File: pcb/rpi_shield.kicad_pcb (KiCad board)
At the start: 2 copper layers, 65 x 56 mm, 60 parts, among them P101 CONN_01X08, P102 CONN_02X20, P301 USB_OTG, Q201 Q_NMOS_GDSD, Q202 Q_NMOS_GDSD, Q203 Q_NMOS_GDSD, Q204 Q_NMOS_GDSD, Q301 FT230XS-R, U201 LM2902N, U202 MAX5813

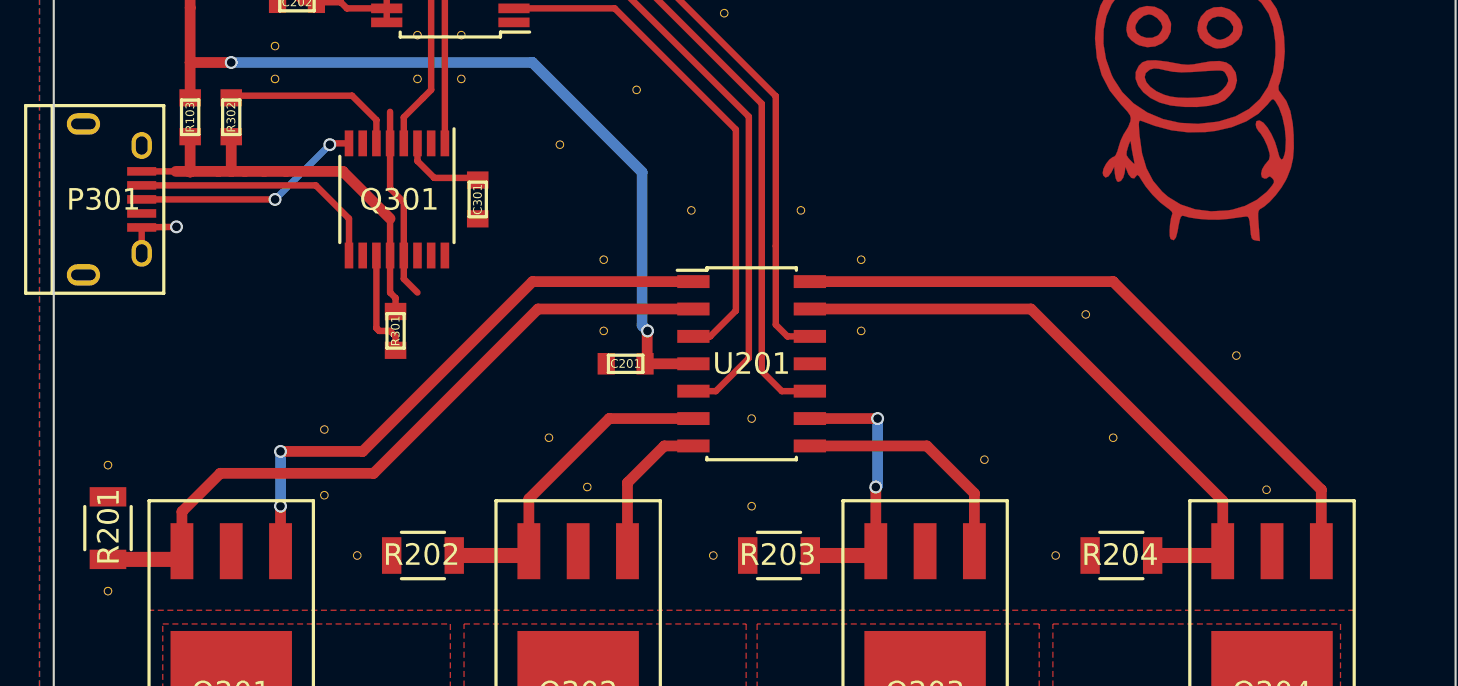
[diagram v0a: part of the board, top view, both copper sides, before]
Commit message: added gain to current feedback
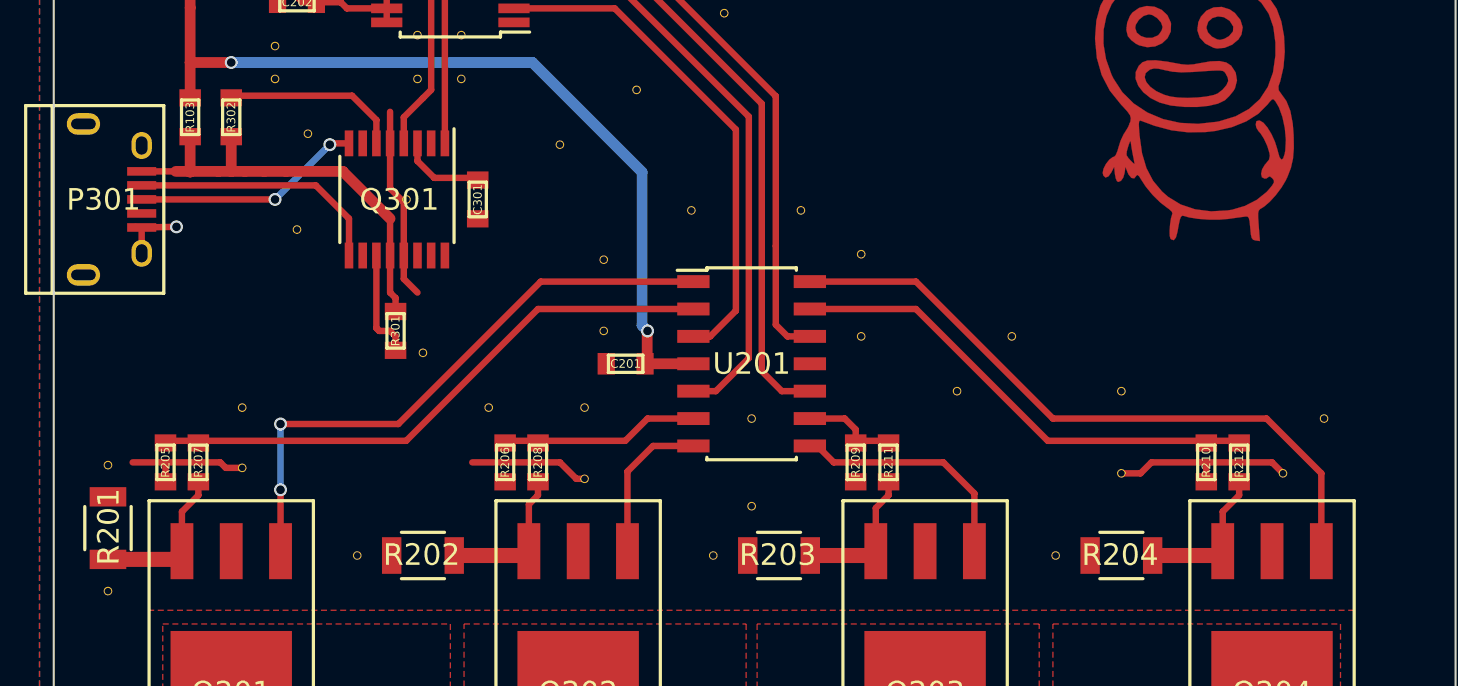
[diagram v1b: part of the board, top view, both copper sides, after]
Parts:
- removed the VIA at (144.7, 106.3)
- removed the VIA at (164.9, 107.3)
- removed the VIA at (170.9, 106.3)
- removed the VIA at (176.6, 102.5)
- removed the VIA at (146.5, 108.6)
- removed the VIA at (178.0, 108.7)
- removed the VIA at (134.3, 105.9)
- removed the VIA at (134.3, 109.0)
- added R205: 1k, netl:SMD_0603, F.Cu at (127.0, 107.4)
- added R206: 1k, netl:SMD_0603, F.Cu at (142.7, 107.4)
- added R207: 10k, netl:SMD_0603, F.Cu at (128.5, 107.4)
- added R208: 10k, netl:SMD_0603, F.Cu at (144.2, 107.4)
- added R209: 1k, netl:SMD_0603, F.Cu at (159.0, 107.4)
- added R210: 1k, netl:SMD_0603, F.Cu at (175.2, 107.4)
- added R211: 10k, netl:SMD_0603, F.Cu at (160.5, 107.4)
- added R212: 10k, netl:SMD_0603, F.Cu at (176.7, 107.4)
- added VIA: via, netl:via, F.Cu at (133.0, 96.6)
- added VIA: via, netl:via, F.Cu at (146.4, 108.2)
- added VIA: via, netl:via, F.Cu at (141.9, 104.9)
- added VIA: via, netl:via, F.Cu at (138.9, 102.4)
- added VIA: via, netl:via, F.Cu at (138.1, 95.2)
- added VIA: via, netl:via, F.Cu at (133.6, 92.2)
- added VIA: via, netl:via, F.Cu at (146.4, 104.9)
- added VIA: via, netl:via, F.Cu at (180.7, 105.4)
- added VIA: via, netl:via, F.Cu at (178.8, 107.9)
- added VIA: via, netl:via, F.Cu at (171.3, 104.1)
- added VIA: via, netl:via, F.Cu at (171.3, 107.9)
- added VIA: via, netl:via, F.Cu at (163.7, 104.1)
- added VIA: via, netl:via, F.Cu at (130.5, 104.9)
- added VIA: via, netl:via, F.Cu at (130.5, 107.7)
- moved VIA 3.58 mm to (166.2, 101.6)
- moved VIA 0.25 mm to (159.2, 97.8)
- moved VIA 0.25 mm to (159.2, 101.6)
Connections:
- U201 pad 13: Net-(Q204-Pad3) -> Net-(R210-Pad1)
- U201 pad 2: Net-(Q201-Pad3) -> Net-(R205-Pad1)
- U201 pad 6: Net-(Q202-Pad3) -> Net-(R206-Pad1)
- U201 pad 9: Net-(Q203-Pad3) -> Net-(R209-Pad1)
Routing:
- net Net-(R205-Pad1): track 0.00 -> 27.0 mm
- net Net-(Q201-Pad3): track 33.3 -> 7.26 mm
- net Net-(R210-Pad1): track 0.00 -> 22.4 mm
- net Net-(Q204-Pad3): track 29.2 -> 7.44 mm
- net GND: track 24.3 -> 44.9 mm
- net Net-(R206-Pad1): track 0.00 -> 9.16 mm
- net Net-(Q202-Pad3): track 15.3 -> 6.99 mm
- net Net-(Q203-Pad3): track 13.5 -> 7.57 mm, vias 2 -> 0
- net Net-(R209-Pad1): track 0.00 -> 4.38 mm
- net Net-(Q201-Pad1): track 27.4 -> 28.1 mm

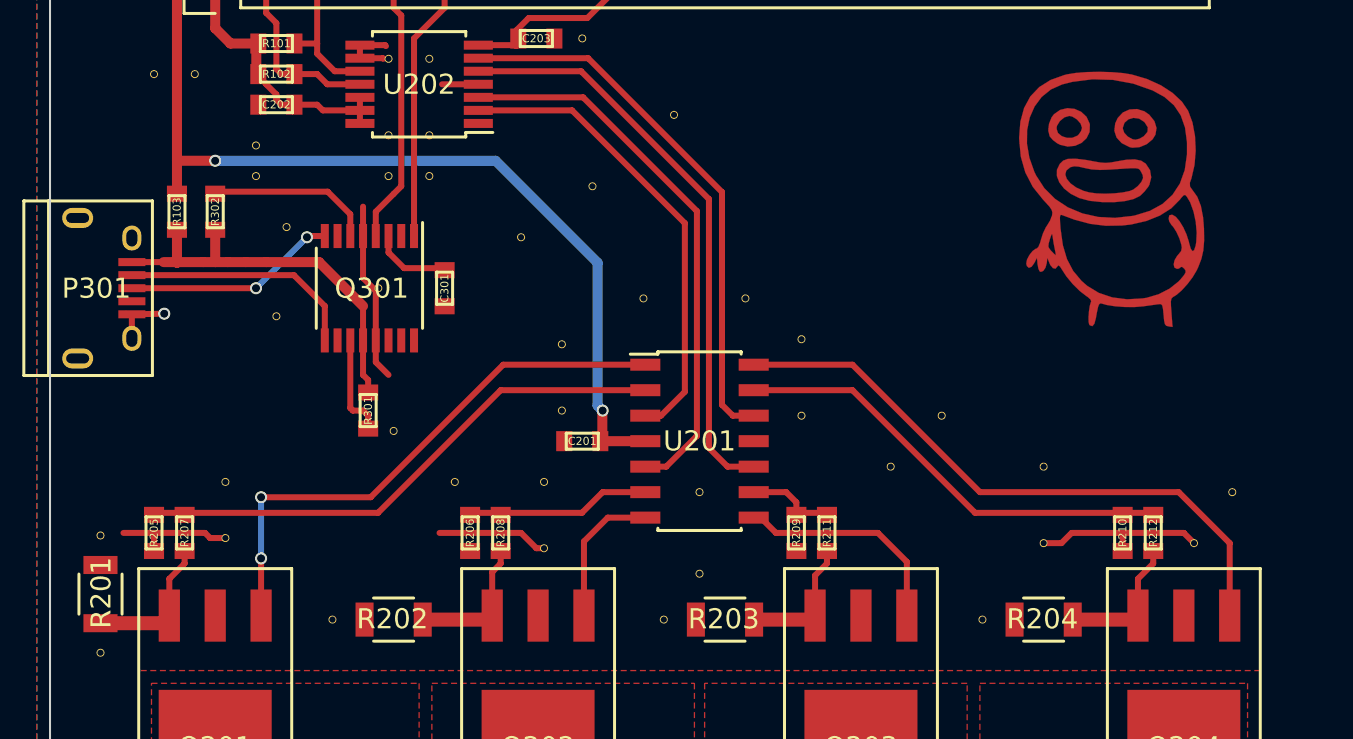
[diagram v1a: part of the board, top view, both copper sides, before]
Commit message: removed gain from feedback, added adjust to DAC reference voltage
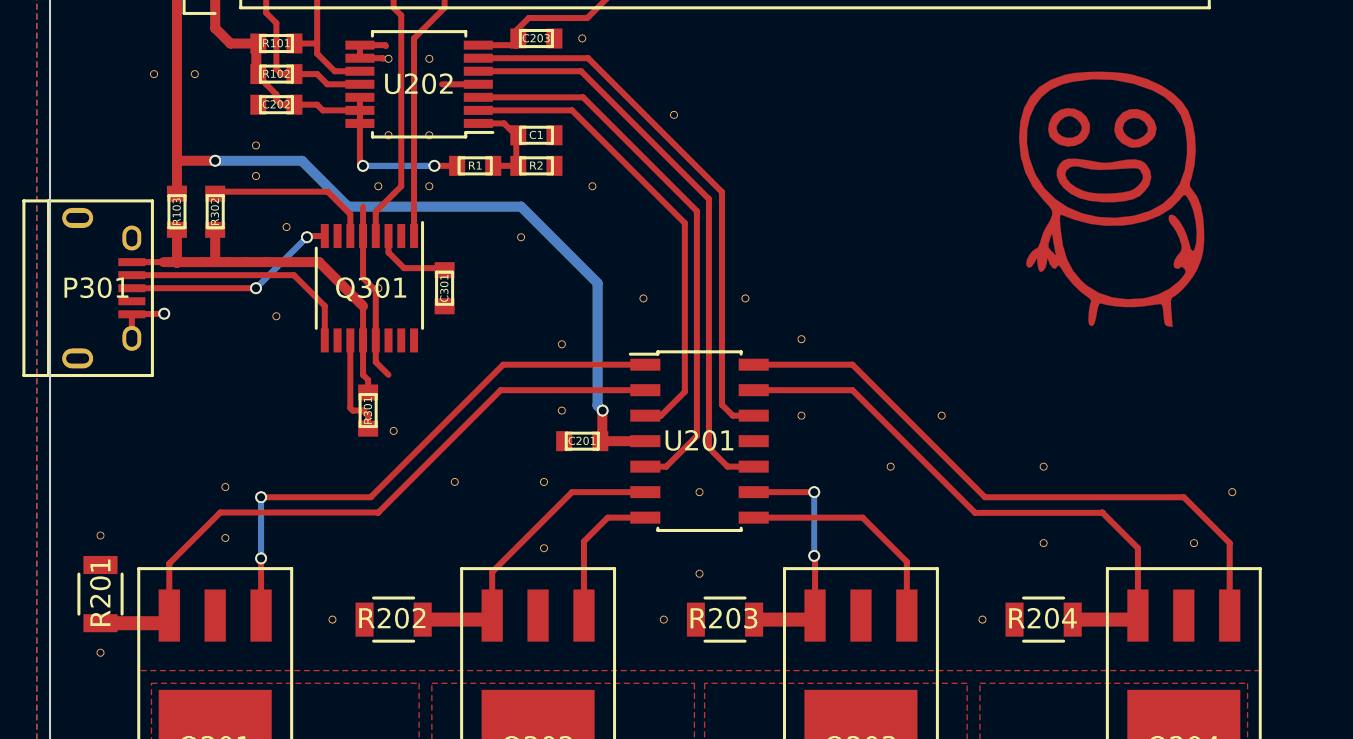
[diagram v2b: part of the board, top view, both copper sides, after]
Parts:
- removed R205, R206, R209, R210: 1k, netl:SMD_0603
- removed R207, R208, R211, R212: 10k, netl:SMD_0603
- added C1: 100n, netl:SMD_0603, F.Cu at (146.0, 87.6)
- added R1: 20k, netl:SMD_0603, F.Cu at (143.0, 89.1)
- added R2: 10k, netl:SMD_0603, F.Cu at (146.0, 89.1)
- moved VIA 0.72 mm to (138.1, 90.2)
- moved VIA 0.51 mm to (140.7, 90.2)
- moved VIA 0.25 mm to (130.5, 105.1)
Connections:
- U201 pad 13: Net-(R210-Pad1) -> Net-(Q204-Pad3)
- U201 pad 2: Net-(R205-Pad1) -> Net-(Q201-Pad3)
- U201 pad 6: Net-(R206-Pad1) -> Net-(Q202-Pad3)
- U201 pad 9: Net-(R209-Pad1) -> Net-(Q203-Pad3)
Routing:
- net Net-(R205-Pad1): track 27.0 -> 0.00 mm
- net Net-(Q201-Pad3): track 7.26 -> 33.7 mm
- net Net-(R210-Pad1): track 22.4 -> 0.00 mm
- net Net-(Q204-Pad3): track 7.44 -> 29.8 mm
- net GND: track 44.9 -> 24.3 mm
- net Net-(R206-Pad1): track 9.16 -> 0.00 mm
- net Net-(Q202-Pad3): track 6.99 -> 15.1 mm
- net 3v3: track 22.6 -> 29.4 mm, vias 0 -> 2
- net Net-(Q203-Pad3): track 7.57 -> 13.4 mm, vias 0 -> 2
- net Net-(C1-Pad2): track 0.00 -> 4.71 mm
- net Net-(R209-Pad1): track 4.38 -> 0.00 mm
- net 5V: track 51.2 -> 50.7 mm

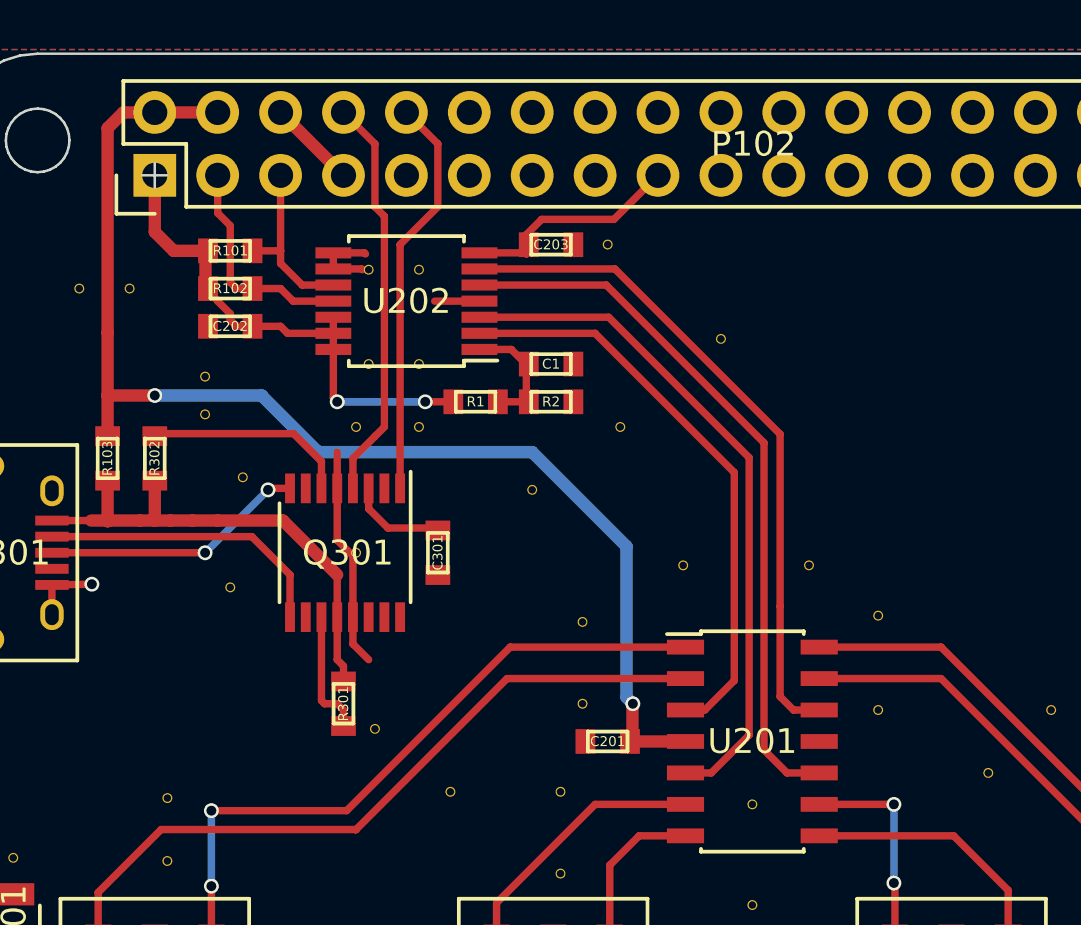
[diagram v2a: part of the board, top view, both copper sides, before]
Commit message: added pulldown transistors, moved reference adjust to DAC output
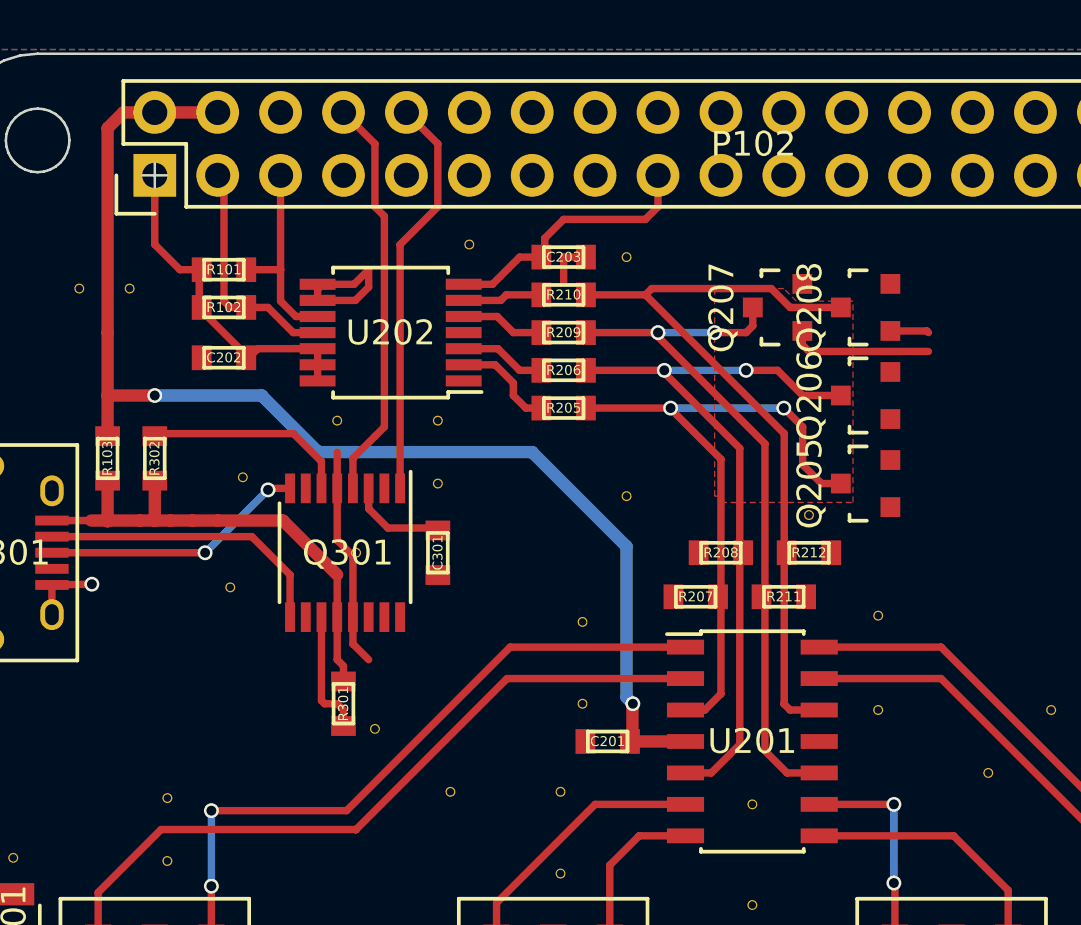
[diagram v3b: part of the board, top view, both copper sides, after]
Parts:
- removed C1: 100n, netl:SMD_0603
- removed R1: 20k, netl:SMD_0603
- removed R2: 10k, netl:SMD_0603
- removed the VIA at (145.2, 92.7)
- removed the VIA at (132.0, 88.1)
- removed the VIA at (132.0, 89.7)
- removed the VIA at (140.7, 87.6)
- removed the VIA at (138.6, 87.6)
- removed the VIA at (148.8, 90.2)
- removed the VIA at (152.9, 86.6)
- removed the VIA at (148.3, 82.8)
- removed the VIA at (138.6, 83.8)
- added Q205: NPN, TO_SOT_Packages_SMD:SOT-23, F.Cu at (158.7, 92.4)
- added Q206: NPN, TO_SOT_Packages_SMD:SOT-23, F.Cu at (158.7, 88.9)
- added Q207: NPN, TO_SOT_Packages_SMD:SOT-23, F.Cu at (155.1, 85.3)
- added Q208: NPN, TO_SOT_Packages_SMD:SOT-23, F.Cu at (158.7, 85.3)
- added R205: 10k, netl:SMD_0603, F.Cu at (146.5, 89.4)
- added R206: 10k, netl:SMD_0603, F.Cu at (146.5, 87.9)
- added R207: 10k, netl:SMD_0603, F.Cu at (151.8, 97.0)
- added R208: 10k, netl:SMD_0603, F.Cu at (152.9, 95.2)
- added R209: 10k, netl:SMD_0603, F.Cu at (146.5, 86.3)
- added R210: 10k, netl:SMD_0603, F.Cu at (146.5, 84.8)
- added R211: 10k, netl:SMD_0603, F.Cu at (155.4, 97.0)
- added R212: 10k, netl:SMD_0603, F.Cu at (156.4, 95.2)
- added VIA: via, netl:via, F.Cu at (149.1, 83.3)
- added VIA: via, netl:via, F.Cu at (141.4, 92.4)
- moved VIA 3.61 mm to (149.1, 93.0)
- moved VIA 2.27 mm to (142.7, 82.8)
- moved VIA 2.03 mm to (156.4, 93.7)
- moved U202 1.42 mm to (139.5, 86.3)
- moved C202 1.30 mm to (132.8, 87.4)
- moved R101 0.80 mm to (132.8, 83.8)
- moved R102 0.80 mm to (132.8, 85.3)
- moved VIA 0.80 mm to (141.4, 89.9)
- moved VIA 0.80 mm to (137.4, 89.9)
- moved C203 0.72 mm to (146.5, 83.3)
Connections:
- net /LED driver/DrainBlue renamed /LED driver/DrainC
- net /LED driver/DrainFan renamed /LED driver/DrainD
- net /LED driver/DrainGreen renamed /LED driver/DrainB
- net /LED driver/DrainRed renamed /LED driver/DrainA
- U201 pad 10: /LED driver/B -> Net-(Q207-Pad3)
- U201 pad 12: /LED driver/W -> Net-(Q208-Pad3)
- U201 pad 3: /LED driver/R -> Net-(Q205-Pad3)
- U201 pad 5: /LED driver/G -> Net-(Q206-Pad3)
- U202 pad 2: /LED driver/R -> /LED driver/A
- U202 pad 3: /LED driver/G -> /LED driver/B
- U202 pad 5: /LED driver/B -> /LED driver/C
- U202 pad 6: /LED driver/W -> /LED driver/D
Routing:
- net Net-(Q208-Pad3): track 0.00 -> 31.0 mm
- net Net-(Q206-Pad3): track 0.00 -> 30.4 mm, vias 0 -> 2
- net Net-(Q207-Pad3): track 0.00 -> 29.2 mm, vias 0 -> 2
- net /LED driver/G: track 27.6 -> 0.00 mm
- net /LED driver/W: track 27.3 -> 0.00 mm
- net Net-(Q205-Pad3): track 0.00 -> 26.5 mm, vias 0 -> 2
- net /LED driver/B: track 29.1 -> 3.40 mm
- net /LED driver/R: track 23.5 -> 0.00 mm
- net Net-(Q207-Pad1): track 0.00 -> 5.77 mm
- net 3v3: track 29.4 -> 24.3 mm, vias 2 -> 0
- net Net-(U202-Pad1): track 4.71 -> 0.00 mm
- net /LED driver/A: track 0.00 -> 4.06 mm
- net /LED driver/C: track 0.00 -> 3.30 mm
- net /LED driver/D: track 0.00 -> 3.13 mm
- net Net-(Q208-Pad1): track 0.00 -> 1.57 mm
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- added copper zone on F.Cu, net /LED driver/DrainBlue
- added copper zone on F.Cu, net /LED driver/DrainFan
- added copper zone on F.Cu, net /LED driver/DrainGreen
- added copper zone on F.Cu, net /LED driver/DrainRed
- removed copper zone on F.Cu, net /LED driver/DrainA
- removed copper zone on F.Cu, net /LED driver/DrainB
- removed copper zone on F.Cu, net /LED driver/DrainC
- removed copper zone on F.Cu, net /LED driver/DrainD

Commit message: cleaned up a bit
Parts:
- removed the VIA at (130.5, 105.1)
- removed the VIA at (130.5, 107.7)
- removed the VIA at (127.0, 84.6)
- removed the VIA at (154.1, 105.4)
- removed the VIA at (166.2, 101.6)
- removed the VIA at (133.0, 96.6)
- removed the VIA at (147.3, 101.3)
- removed the VIA at (146.4, 104.9)
- removed the VIA at (180.7, 105.4)
- removed the VIA at (178.8, 107.9)
- removed the VIA at (171.3, 104.1)
- removed the VIA at (163.7, 104.1)
- added G***: LOGO, netl:LOGO_127mm, F.Cu at (174.7, 90.9)
- added VIA: via, netl:via, F.Cu at (178.0, 108.2)
- moved VIA 2.90 mm to (144.7, 104.1)
- moved VIA 2.18 mm to (146.0, 96.3)
- moved VIA 2.05 mm to (139.9, 100.6)
- moved VIA 1.44 mm to (130.0, 85.6)
- moved VIA 1.37 mm to (159.7, 102.9)
- moved VIA 1.27 mm to (151.1, 111.8)
- moved VIA 1.14 mm to (167.1, 111.8)
- moved VIA 1.14 mm to (159.7, 96.8)
- moved VIA 1.02 mm to (134.8, 111.8)
- moved VIA 1.02 mm to (132.5, 92.2)
- moved VIA 1.02 mm to (154.1, 108.4)
- moved VIA 0.92 mm to (149.6, 92.2)
- moved VIA 0.77 mm to (171.4, 108.7)
- moved VIA 0.63 mm to (146.8, 108.7)
- moved G*** 0.14 mm to (174.7, 90.9)
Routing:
- net Net-(Q205-Pad1): track 0.00 -> 1.62 mm
- net Net-(Q206-Pad1): track 0.00 -> 1.57 mm
- net GND: track 23.7 -> 25.3 mm
- added copper zone on F.Cu, net /LED driver/DrainA
- added copper zone on F.Cu, net /LED driver/DrainB
- added copper zone on F.Cu, net /LED driver/DrainC
- added copper zone on F.Cu, net /LED driver/DrainD
- removed copper zone on F.Cu, net /LED driver/DrainBlue
- removed copper zone on F.Cu, net /LED driver/DrainFan
- removed copper zone on F.Cu, net /LED driver/DrainGreen
- removed copper zone on F.Cu, net /LED driver/DrainRed
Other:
- board text added: "+"
- board text added: "A"
- board text added: "B"
- board text added: "C"
- board text added: "D"
- board text added: "GND"
